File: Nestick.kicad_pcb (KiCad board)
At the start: 2 copper layers, 20 parts, among them J1 CONN_EXT, J2 CONN_DIRS, J3 CONN_DGND, J4 CONN_BTNS, J5 CONN_BGND, Q1 2N3904, U1 74LS165, U2 74LS165

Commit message: Dress up for release
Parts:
- removed REF** (x4): MountingHole_2.1mm, MountingHole:MountingHole_2.1mm
- added H1: HOLE, MountingHole:MountingHole_3.2mm_M3_Pad, F.Cu at (103.9, 148.3)
- added H2: HOLE, MountingHole:MountingHole_3.2mm_M3_Pad, F.Cu at (145.4, 148.3)
- added H3: HOLE, MountingHole:MountingHole_3.2mm_M3_Pad, F.Cu at (145.4, 103.3)
- added H4: HOLE, MountingHole:MountingHole_3.2mm_M3_Pad, F.Cu at (103.9, 103.3)
- moved Q1 0.51 mm to (137.5, 111.7)
- moved C2 0.34 mm to (137.5, 102.5)
- moved C1 0.05 mm to (137.5, 138.1)
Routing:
- net VCC: track 122.0 -> 121.2 mm
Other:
- board outline added: 50.5 x 53.8 mm
- board text added: "+5V"
- board text added: "B (A)"
- board text added: "CLK"
- board text added: "D0"
- board text added: "GND"
- board text added: "LCH"
- board text added: "NES"
- board text added: "NES/SNES Controller Board"
- board text added: "NESTIK"
- board text added: "SNES"
- board text added: "Y (B)"
- board text removed: "B"
- board text removed: "Y"

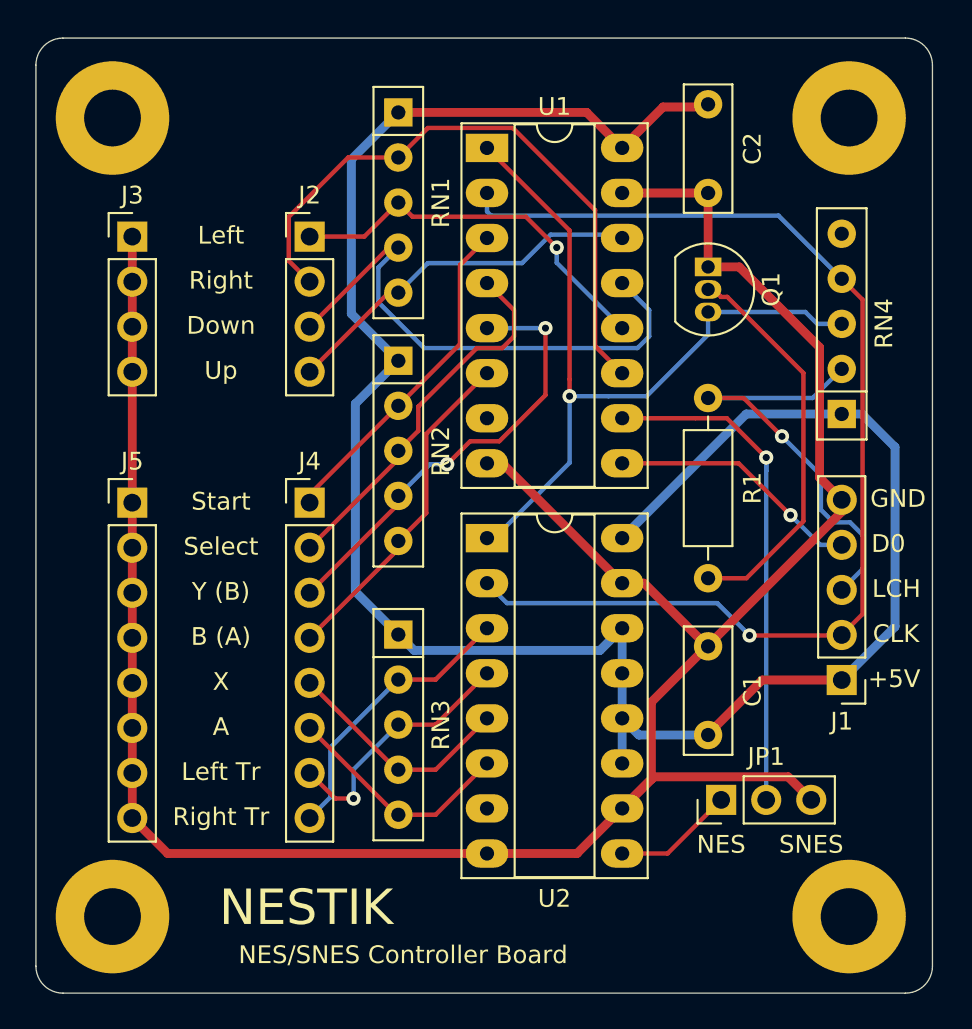
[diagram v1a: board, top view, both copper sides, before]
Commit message: Back to 50x50mm
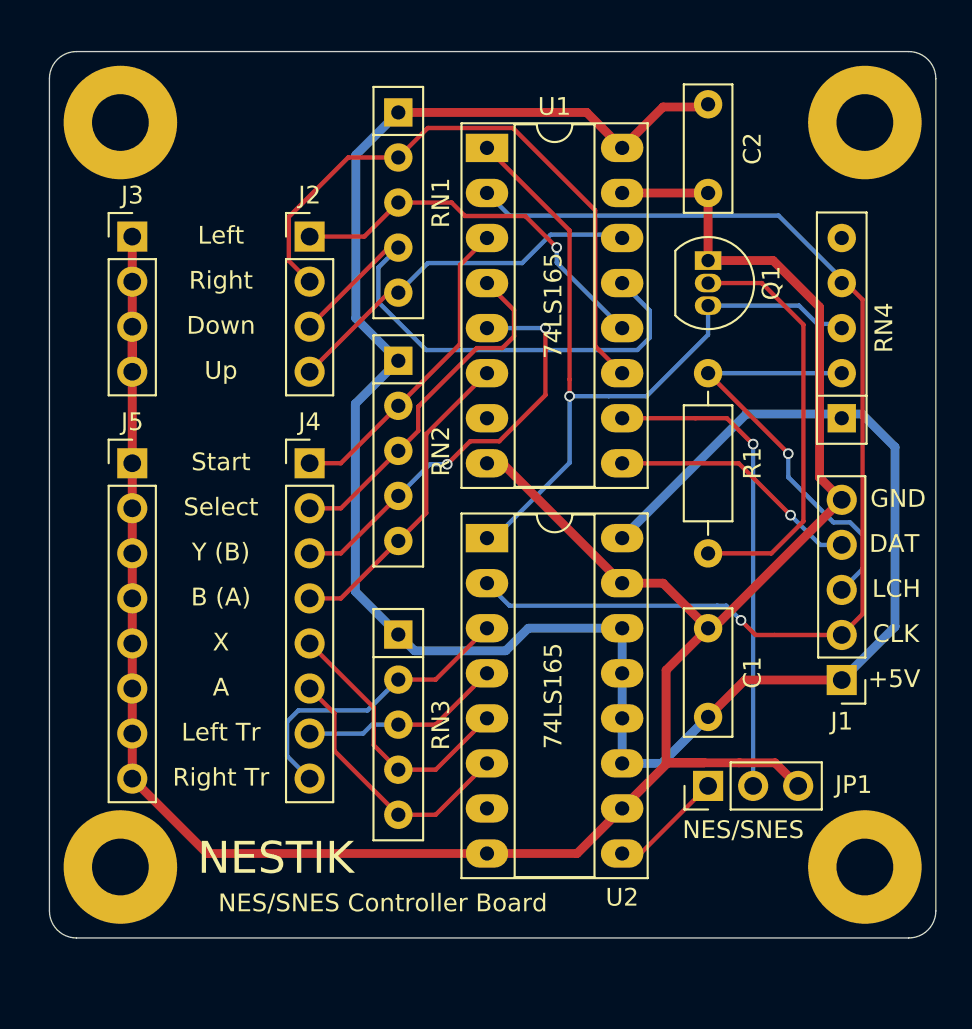
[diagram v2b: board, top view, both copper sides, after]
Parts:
- moved H2 2.93 mm to (146.3, 145.5)
- moved H1 2.83 mm to (104.3, 145.5)
- moved J4 2.22 mm to (115.0, 122.8)
- moved J5 2.22 mm to (105.0, 122.8)
- moved R1 1.40 mm to (137.5, 127.9)
- moved JP1 1.08 mm to (137.5, 141.0)
- moved C1 1.02 mm to (137.5, 137.1)
- moved H3 0.92 mm to (146.3, 103.6)
- moved H4 0.51 mm to (104.3, 103.6)
- moved Q1 0.36 mm to (137.5, 111.3)
- moved RN4 0.24 mm to (145.0, 120.2)
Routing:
- net /btn_fl: track 14.5 -> 11.4 mm, vias 1 -> 0
- net /btn_a: track 13.2 -> 15.5 mm
- net /btn_x: track 13.2 -> 15.4 mm
- net Net-(Q1-Pad2): track 22.0 -> 23.6 mm
- net Net-(JP1-Pad2): track 28.7 -> 27.2 mm
- net /btn_st: track 19.1 -> 17.9 mm
- net /btn_fr: track 16.1 -> 17.2 mm
- net /btn_y: track 25.3 -> 24.5 mm
- net /btn_sel: track 21.2 -> 20.4 mm
- net /btn_b: track 19.1 -> 18.3 mm
- net /clock: track 64.9 -> 64.3 mm
- net GND: track 139.4 -> 139.9 mm
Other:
- board size 50.5 x 53.8 mm -> 50 x 50 mm
- net class Default: via_dia 0.8 -> 0.6
- net class Powah added: clearance 0.2, trace_width 0.5, via_dia 0.8, via_drill 0.6
- board text added: "DAT"
- board text added: "NES/SNES"
- board text removed: "D0"
- board text removed: "NES"
- board text removed: "SNES"
